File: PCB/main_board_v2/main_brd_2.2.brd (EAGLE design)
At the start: 87.5 x 79 mm, 53 parts, among them J2 SD-card Adapter, J3 E-paper Module, J4 Zigbee Module, J5 BATT, J6 CHARGER, J7 POGO_PINS, J8 ST-LINK, J9 additional I2C bus, U1 STM32F103C8T6-MODULE, U2 LF411CP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

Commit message: Created board 2.2
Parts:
- added C7: 100u, rcl:C025-050X050
- added JP1: (no value), pinhead:1X02
- added R16, R17: 10k, eagle-ltspice:R0603
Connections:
- new net REED_MODE: JP1.1, R17.2, U1.PA_12
- new net WET_MODE: JP1.2, R16.2, U1.PA_11
- net GND: now also C7.2, R16.1, R17.1
- net LDO1_3.3V: now also C7.1
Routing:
- net REED_MODE: track 0.00 -> 37.8 mm
- net WET_MODE: track 0.00 -> 37.7 mm
- net LDO1_3.3V: track 124.5 -> 125.4 mm
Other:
- board text added: "BAT_OUT"
- board text added: "Battery Disconnect"
- board text added: "OUT+"
- board text added: "OUT-"

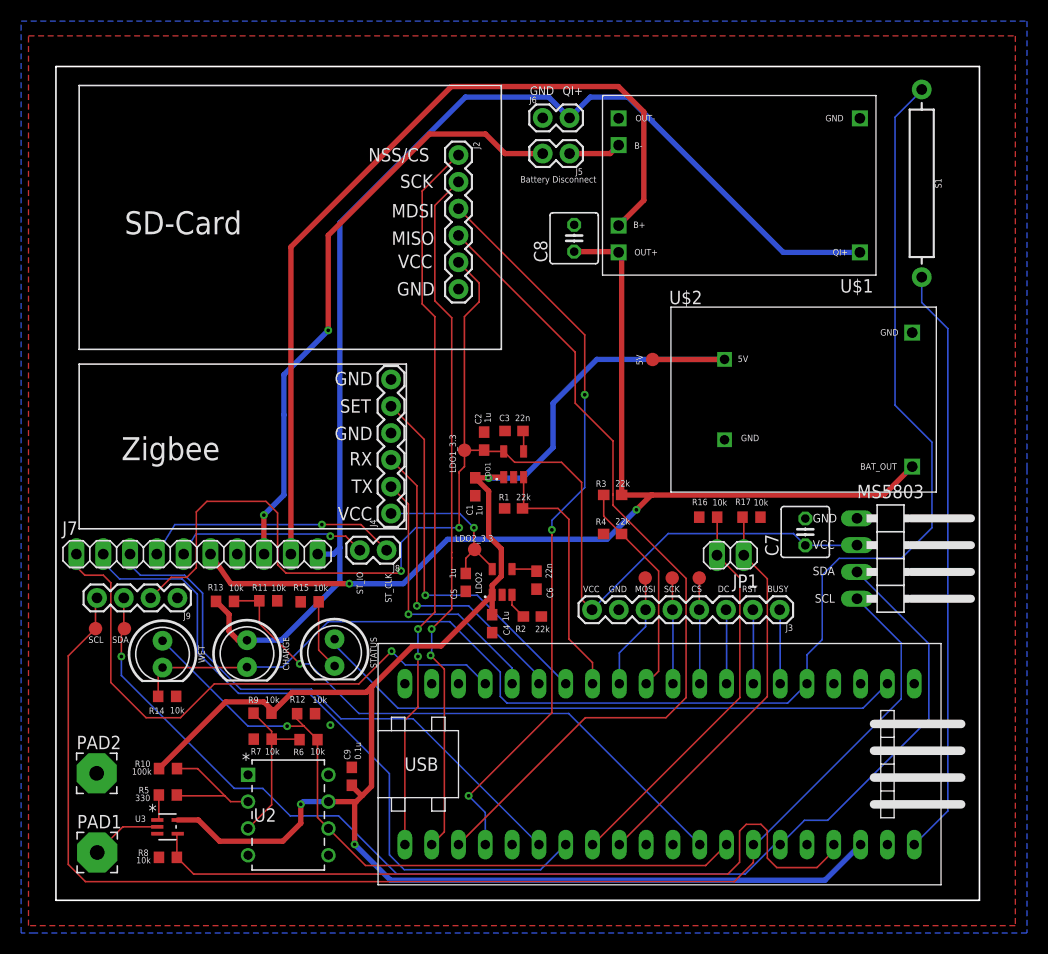
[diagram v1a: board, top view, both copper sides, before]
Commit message: Fixed wkup and routing
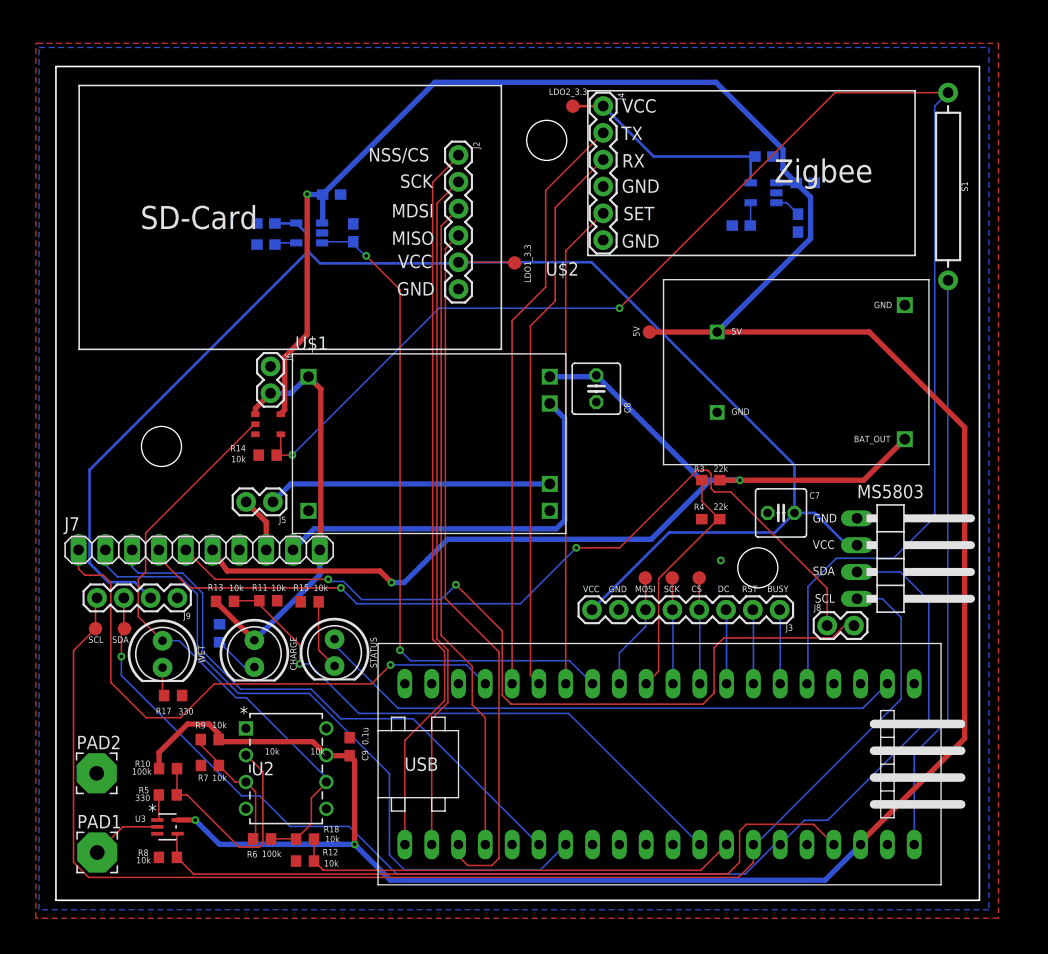
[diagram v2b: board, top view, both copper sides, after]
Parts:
- removed JP1: (no value), pinhead:1X02
- added R18: 10k, eagle-ltspice:R0603
- added U$3: 74LVC1G86SE-7, coral_power:SOT25
- R16, R17: value 10k -> 330
- moved R17 57.3 mm to (11.1, 19.4), turned to 0 degrees
- moved C4 51.2 mm to (71.0, 68.0), flipped to the bottom, turned to 180 degrees
- moved C5 49.3 mm to (67.1, 70.5), flipped to the bottom, turned to 180 degrees
- moved R16 47.6 mm to (15.5, 25.3), flipped to the bottom, turned to 90 degrees
- moved R2 45.0 mm to (70.3, 64.2), flipped to the bottom, turned to 90 degrees
- moved LDO2 44.4 mm to (67.0, 67.0), flipped to the bottom, turned to 0 degrees
- moved J4 43.5 mm to (51.9, 75.2), turned to 270 degrees
- moved J5 43.3 mm to (20.6, 37.8)
- moved TP5 43.0 mm to (49.0, 75.2)
- moved J8 42.3 mm to (73.1, 26.0), turned to 0 degrees
- moved C6 38.8 mm to (64.9, 63.9), flipped to the bottom, turned to 0 degrees
- moved U$1 38.2 mm to (35.4, 43.3), turned to 0 degrees
- moved J6 34.9 mm to (20.3, 50.6), turned to 270 degrees
- moved C1 30.9 mm to (26.1, 66.9), flipped to the bottom, turned to 180 degrees
- moved R1 30.2 mm to (28.2, 63.2), flipped to the bottom, turned to 270 degrees
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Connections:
- removed net REED_MODE: JP1.1, R17.2, U1.PA_12
- removed net WET_MODE: JP1.2, R16.2, U1.PA_11
- new net N$10: R17.1, WET.K
- new net N$3: CHARGE.K, R16.1
- new net WET_WKUP: R18.1, R6.2, U$3.P$2, U2.6, WET.A
- net +5V: now also U$3.P$4
- net GND: now also R16.2, R17.2, U$3.P$3; no longer R16.1, R17.1
- net QI+: now also U$3.P$1
- net READ_WET: now also R18.2; no longer R6.2, U2.6, WET.A
- net WKUP: now also U$3.P$5; no longer CHARGE.K, WET.K
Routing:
- net +5V: track 181.1 -> 277.2 mm
- net QI+: track 114.8 -> 40.1 mm
- net ST_CLK: track 18.4 -> 79.7 mm, vias 1 -> 2
- net WET_WKUP: track 0.00 -> 56.4 mm
- net ST_IO: track 24.3 -> 80.1 mm, vias 1 -> 2
- net B+1: track 57.8 -> 5.34 mm, vias 2 -> 0
- net B+0: track 81.6 -> 38.6 mm
- net LDO1_EN: track 24.3 -> 63.2 mm, vias 0 -> 2
- net REED_MODE: track 37.8 -> 0.00 mm
- net WET_MODE: track 37.7 -> 0.00 mm
- net ZIGBEE_TX: track 26.2 -> 55.8 mm, vias 1 -> 0
- net READ_WET: track 68.9 -> 42.5 mm, vias 1 -> 0
- net ZIGBEE_RX: track 29.9 -> 52.8 mm, vias 1 -> 0
- net B-: track 4.98 -> 26.9 mm
- net LDO1_3.3V: track 125.4 -> 145.1 mm, vias 2 -> 0
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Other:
- board text removed: "B+"
- board text removed: "B-"
- board text removed: "Battery Disconnect"
- board text removed: "OUT+"
- board text removed: "OUT-"
- board text removed: "QI+"
- board text removed: "ST_CLK"
- board text removed: "ST_IO"
